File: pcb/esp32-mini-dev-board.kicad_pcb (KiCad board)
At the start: 2 copper layers, 39.9 x 52 mm, 11 parts, among them J1 USB_C_Receptacle_USB2.0_16P, U1 USBLC6-2SC6, U2 AP2112K-3.3, U3 ESP32-C3-WROOM-02

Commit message: feat(lay): add first placement of all parts
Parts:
- added C10: 100n, Capacitor_SMD:C_0603_1608Metric, B.Cu at (157.0, 100.9)
- added C11: C, Capacitor_SMD:C_0603_1608Metric, F.Cu at (173.2, 125.4)
- added C5: C, Capacitor_SMD:C_0603_1608Metric, B.Cu at (161.6, 99.7)
- added C6: 4u7, Capacitor_SMD:C_0603_1608Metric, F.Cu at (162.1, 117.8)
- added C7: C, Capacitor_SMD:C_0603_1608Metric, B.Cu at (161.5, 102.3)
- added C8: 4u7, Capacitor_SMD:C_0603_1608Metric, F.Cu at (159.6, 114.6)
- added C9: 4u7, Capacitor_SMD:C_0603_1608Metric, B.Cu at (157.1, 99.2)
- added J2: Conn_01x08_Pin, Connector_PinHeader_2.54mm:PinHeader_1x08_P2.54mm_Vertical, B.Cu at (150.0, 100.0)
- added J3: Conn_01x08_Pin, Connector_PinHeader_2.54mm:PinHeader_1x08_P2.54mm_Vertical, B.Cu at (176.0, 100.0)
- added R10: R, Resistor_SMD:R_0603_1608Metric, F.Cu at (154.0, 114.9)
- added R11: R, Resistor_SMD:R_0603_1608Metric, F.Cu at (173.2, 127.2)
- added R3: R, Resistor_SMD:R_0603_1608Metric, F.Cu at (150.6, 123.6)
- added R4: R, Resistor_SMD:R_0603_1608Metric, F.Cu at (149.7, 121.2)
- added R5: 0R, Resistor_SMD:R_0603_1608Metric, F.Cu at (160.9, 119.5)
- added R6: 0R, Resistor_SMD:R_0603_1608Metric, B.Cu at (168.8, 100.3)
- added R7: R, Resistor_SMD:R_0603_1608Metric, B.Cu at (166.5, 101.1)
- added R8: 0R, Resistor_SMD:R_0603_1608Metric, B.Cu at (168.8, 101.8)
- added R9: R, Resistor_SMD:R_0603_1608Metric, F.Cu at (171.8, 114.8)
- added SW1: SW_Push, Button_Switch_SMD:SW_SPST_B3U-1000P, F.Cu at (153.0, 130.0)
- added SW2: SW_Push, Button_Switch_SMD:SW_SPST_B3U-1000P, F.Cu at (173.0, 130.0)
- added Y1: Crystal, Crystal:Crystal_SMD_3215-2Pin_3.2x1.5mm, B.Cu at (164.3, 101.0)
- C1: value 4u7 -> C; footprint Diode_SMD:D_SMA -> Capacitor_SMD:C_0603_1608Metric
- C2: footprint Diode_SMD:D_SMA -> Capacitor_SMD:C_0603_1608Metric
- C3: value 4u7 -> C; footprint Package_TO_SOT_SMD:SOT-23-5 -> Capacitor_SMD:C_0603_1608Metric
- C4: footprint Package_TO_SOT_SMD:SOT-23-5 -> Capacitor_SMD:C_0603_1608Metric
- R1, R2: footprint Resistor_SMD:R_0402_1005Metric -> Resistor_SMD:R_0603_1608Metric
- moved J1 37.2 mm to (163.0, 131.0)
- moved U2 35.5 mm to (162.2, 114.7), turned to 90 degrees
- moved U3 32.2 mm to (163.0, 104.7)
- moved U1 26.2 mm to (162.7, 122.9), turned to 90 degrees
- moved C2 25.6 mm to (157.6, 121.2), turned to 180 degrees
- moved D1 25.0 mm to (154.1, 122.1), turned to 90 degrees
- moved C4 21.6 mm to (157.6, 119.5), turned to 180 degrees
- moved R1 19.3 mm to (165.3, 124.4), turned to 90 degrees
- moved R2 15.1 mm to (160.1, 124.4), turned to 90 degrees
- moved C1 14.5 mm to (149.7, 126.0), turned to 180 degrees
- moved C3 9.33 mm to (149.0, 123.6), turned to -90 degrees
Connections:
- net Net-(U2-EN) renamed +5V
- C1 pad 1: Net-(D1-A1) -> Net-(C1-Pad1)
- C2 pad 1: Net-(C2-Pad1) -> Net-(D1-A1)
- C3 pad 1: Net-(U2-VOUT) -> /CIRCUIT DESIGN/EN_RST
- U1 pad 4: USB_D+ -> /CIRCUIT DESIGN/USB_D+
- U1 pad 6: USB_D- -> /CIRCUIT DESIGN/USB_D-
- U2 pad 5: Net-(U2-VOUT) -> +3V3
- U3 pad 1: unconnected-(U3-3V3-Pad1) -> +3V3
- U3 pad 10: unconnected-(U3-IO10-Pad10) -> /CIRCUIT DESIGN/IO10
- U3 pad 11: unconnected-(U3-IO20/RXD-Pad11) -> /CIRCUIT DESIGN/RXD
- U3 pad 12: unconnected-(U3-IO21/TXD-Pad12) -> /CIRCUIT DESIGN/TXD
- U3 pad 13: unconnected-(U3-IO18-Pad13) -> /CIRCUIT DESIGN/USB_D-
- U3 pad 14: unconnected-(U3-IO19-Pad14) -> /CIRCUIT DESIGN/USB_D+
- U3 pad 15: unconnected-(U3-IO3-Pad15) -> /CIRCUIT DESIGN/IO3
- U3 pad 16: unconnected-(U3-IO2-Pad16) -> Net-(U3-IO2)
- U3 pad 17: unconnected-(U3-IO1-Pad17) -> /CIRCUIT DESIGN/XTAL_32K_N
- U3 pad 18: unconnected-(U3-IO0-Pad18) -> /CIRCUIT DESIGN/XTAL_32K_P
- U3 pad 19: Net-(U3-GND-Pad19) -> GND
- U3 pad 2: unconnected-(U3-EN-Pad2) -> /CIRCUIT DESIGN/EN
- U3 pad 3: unconnected-(U3-IO4-Pad3) -> /CIRCUIT DESIGN/IO4
- U3 pad 4: unconnected-(U3-IO5-Pad4) -> /CIRCUIT DESIGN/IO5
- U3 pad 5: unconnected-(U3-IO6-Pad5) -> /CIRCUIT DESIGN/IO6
- U3 pad 6: unconnected-(U3-IO7-Pad6) -> /CIRCUIT DESIGN/IO7
- U3 pad 7: unconnected-(U3-IO8-Pad7) -> Net-(U3-IO8)
- U3 pad 8: unconnected-(U3-IO9-Pad8) -> /CIRCUIT DESIGN/BOOT
- U3 pad 9: Net-(U3-GND-Pad19) -> GND
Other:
- board size 39.9 x 52 mm -> 31 x 37.4 mm

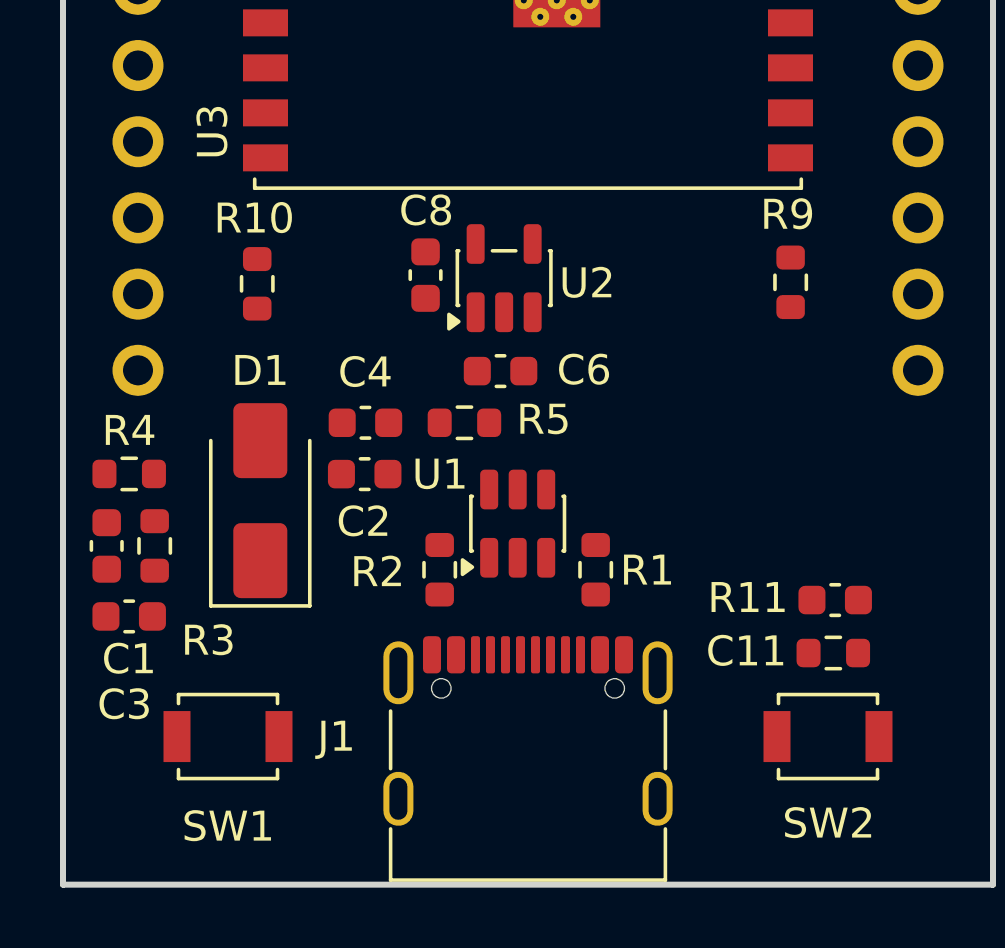
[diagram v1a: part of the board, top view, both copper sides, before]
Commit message: feat(lay): modify placement and first pre-routing
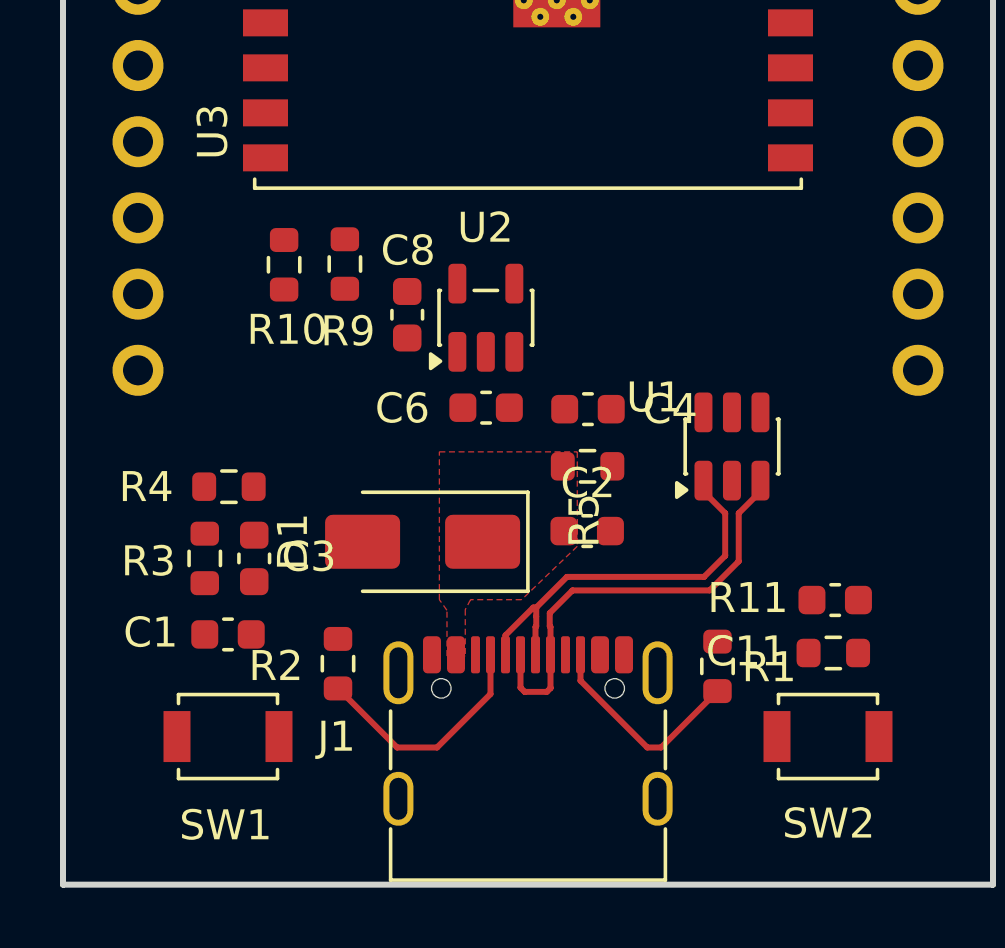
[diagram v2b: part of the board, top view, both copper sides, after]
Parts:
- moved R9 14.9 mm to (156.9, 114.2), turned to 90 degrees
- moved C2 7.66 mm to (165.0, 123.1), turned to 0 degrees
- moved U1 7.59 mm to (169.8, 120.3)
- moved C4 7.43 mm to (165.0, 119.1), turned to 0 degrees
- moved D1 5.58 mm to (159.5, 123.5), turned to 180 degrees
- moved R1 5.18 mm to (169.3, 127.6)
- moved C3 4.94 mm to (153.9, 124.0)
- moved R2 4.61 mm to (156.7, 127.6)
- moved R5 4.35 mm to (165.0, 121.0), turned to 0 degrees
- moved R4 3.35 mm to (153.0, 121.7), turned to 180 degrees
- moved C1 3.35 mm to (153.0, 126.6), turned to 0 degrees
- moved R3 1.72 mm to (152.2, 124.0)
- moved C8 1.45 mm to (159.0, 115.9)
- moved U2 1.45 mm to (161.6, 116.0)
- moved C6 1.31 mm to (161.6, 119.0), turned to 180 degrees
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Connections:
- net Net-(D1-A1) renamed /CIRCUIT DESIGN/VBUS
- R11 pad 1: +VDD -> +3V3
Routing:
- net /CIRCUIT DESIGN/D+: track 0.00 -> 14.7 mm
- net /CIRCUIT DESIGN/D-: track 0.00 -> 13.5 mm
- net Net-(J1-CC1): track 0.00 -> 7.95 mm
- net Net-(J1-CC2): track 0.00 -> 7.13 mm
- added copper zone on F.Cu, net /CIRCUIT DESIGN/VBUS

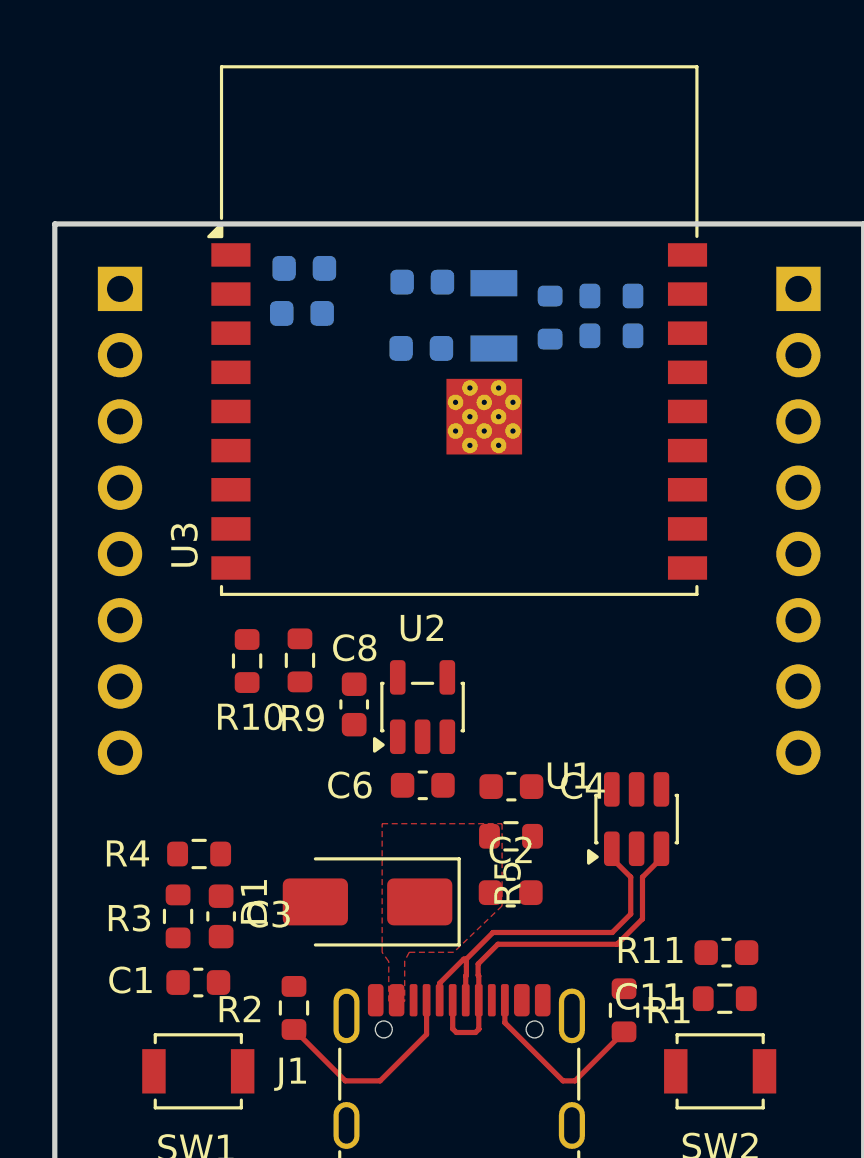
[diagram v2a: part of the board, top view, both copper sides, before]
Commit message: feat(lay/pwr): add +3V3 power zones in F.Cu
- Design rules were set to meet the JLCPCB manufacturing capabilities.
- The +5 and VBUS power zones in F.Cu were fixed to pass DRC.
- Vias for GND, +5V, +3V3 and VBUS were added.
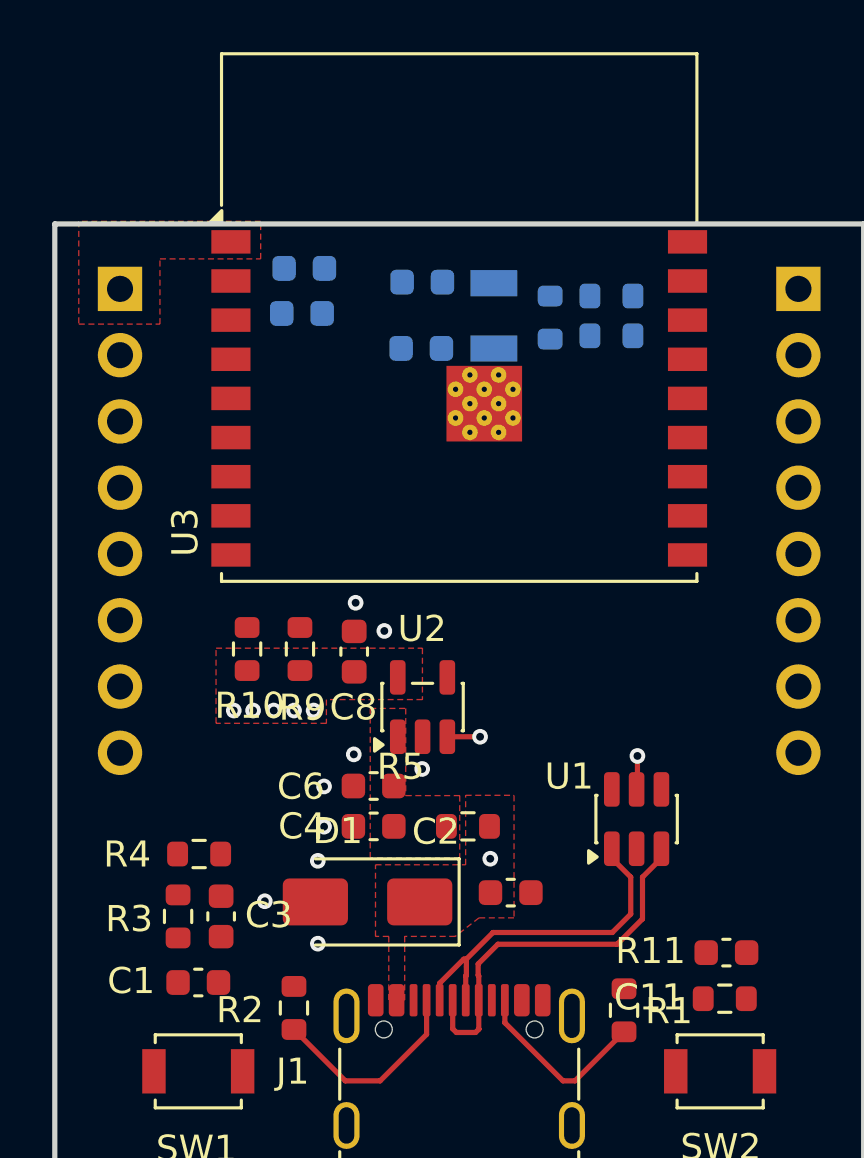
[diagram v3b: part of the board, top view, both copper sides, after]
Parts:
- moved C4 5.49 mm to (159.7, 120.6), turned to 180 degrees
- moved C8 2.03 mm to (159.0, 113.9), turned to 90 degrees
- moved C6 1.88 mm to (159.7, 119.1)
- moved R5 1.69 mm to (163.3, 120.6), turned to 180 degrees
- moved U3 0.50 mm to (163.0, 104.2)
- moved R10 0.46 mm to (154.9, 113.8)
- moved R9 0.43 mm to (156.9, 113.8)
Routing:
- net /CIRCUIT DESIGN/VBUS: track 0.00 -> 1.30 mm, vias 0 -> 2
- net +5V: track 0.00 -> 1.26 mm, vias 0 -> 1
- net GND: vias 0 -> 9
- net +3V3: vias 0 -> 5
- added copper zone on F.Cu, net +3V3
- added copper zone on F.Cu, net +5V
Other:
- copper layers 2 -> 4

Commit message: feat(lay/mcu): add copper zones to connect +3V3 pads to bypass capacitors
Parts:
- moved C10 2.99 mm to (155.0, 98.7)
- moved C9 2.38 mm to (155.0, 100.5)
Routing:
- net +3V3: vias 5 -> 9
- added copper zone on B.Cu, net +3V3
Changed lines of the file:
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@@
 		(capping no)
 		(filling no)
-		(zone_defaults)
 		(pcbplotparams
 			(layerselection 0x00000000_00000000_55555555_5755f5ff)
@@
 	(footprint "Capacitor_SMD:C_0603_1608Metric"
 		(layer "B.Cu")
-		(at 157.0612 99.2126)
+		(at 155.04 100.46)
 		(descr "Capacitor SMD 0603 (1608 Metric), square (rectangular) end terminal, IPC-7351 nominal, (Body size source: IPC-SM-782 page 76, https://www.pcb-3d.com/wordpress/wp-content/uploads/ipc-sm-782a_amendment_1_and_2.pdf)")
 		(tags "capacitor")
@@
 	(footprint "Capacitor_SMD:C_0603_1608Metric"
 		(layer "B.Cu")
-		(at 156.9726 100.9398)
+		(at 155.04 98.6598)
 		(descr "Capacitor SMD 0603 (1608 Metric), square (rectangular) end terminal, IPC-7351 nominal, (Body size source: IPC-SM-782 page 76, https://www.pcb-3d.com/wordpress/wp-content/uploads/ipc-sm-782a_amendment_1_and_2.pdf)")
 		(tags "capacitor")
@@
 	)
 	(via
+		(at 152.84 98.07)
+		(size 0.6)
+		(drill 0.3)
+		(layers "F.Cu" "B.Cu")
+		(free yes)
+		(net "+3V3")
+	)
+	(via
 		(at 157.42 116.16)
 		(size 0.6)
@@
 	)
 	(via
+		(at 152.09 98.07)
+		(size 0.6)
+		(drill 0.3)
+		(layers "F.Cu" "B.Cu")
+		(free yes)
+		(net "+3V3")
+	)
+	(via
 		(at 155.1 116.16)
 		(size 0.6)
@@
 	)
 	(via
+		(at 152.86 98.79)
+		(size 0.6)
+		(drill 0.3)
+		(layers "F.Cu" "B.Cu")
+		(free yes)
+		(net "+3V3")
+	)
+	(via
 		(at 155.89 116.16)
 		(size 0.6)
@@
 	)
 	(via
+		(at 152.09 98.74)
+		(size 0.6)
+		(drill 0.3)
+		(layers "F.Cu" "B.Cu")
+		(free yes)
+		(net "+3V3")
+	)
+	(via
 		(at 154.36 116.16)
 		(size 0.6)
@@
 		(polygon
 			(pts
-				(xy 157.91 115.74) (xy 157.91 116.65) (xy 153.68 116.65) (xy 153.68 113.77) (xy 161.59 113.77) (xy 161.59 115.74)
+				(xy 157.91 115.74) (xy 157.91 116.87) (xy 153.68 116.87) (xy 153.68 113.77) (xy 161.59 113.77) (xy 161.59 115.74)
 			)
 		)
@@
 		(polygon
 			(pts
-				(xy 148.42 97.41) (xy 148.42 101.35) (xy 151.53 101.35) (xy 151.53 98.85) (xy 155.39 98.85) (xy 155.39 97.41)
+				(xy 148.42 97.41) (xy 148.42 101.35) (xy 151.91 101.35) (xy 151.91 99.15) (xy 156.31 99.15) (xy 156.31 97.41)
 			)
 		)
@@
 			)
 		)
+	)
+	(zone
+		(net "+3V3")
+		(layer "B.Cu")
+		(hatch none 0.5)
+		(priority 5)
+		(connect_pads
+			(clearance 0)
+		)
+		(min_thickness 0.2)
+		(fill yes
+			(thermal_gap 0.15)
+			(thermal_bridge_width 0.25)
+			(smoothing fillet)
+			(radius 0.5)
+			(island_removal_mode 1)
+		)
+		(polygon
+			(pts
+				(xy 157.95 116.825) (xy 157.95 115.55) (xy 155.15 115.55) (xy 155.15 101.325) (xy 151.375 101.325)
+				(xy 151.75 101.325) (xy 151.75 116.825)
+			)
+		)
+	)
+	(zone
+		(net "+3V3")
+		(layer "B.Cu")
+		(hatch none 0.5)
+		(priority 4)
+		(connect_pads
+			(clearance 0)
+		)
+		(min_thickness 0.2)
+		(fill yes
+			(thermal_gap 0.15)
+			(thermal_bridge_width 0.25)
+			(smoothing fillet)
+			(radius 0.5)
+			(island_removal_mode 1)
+		)
+		(polygon
+			(pts
+				(xy 155.15 101.325) (xy 155.15 97.7) (xy 148.025 97.7) (xy 148.025 101.325)
+			)
+		)

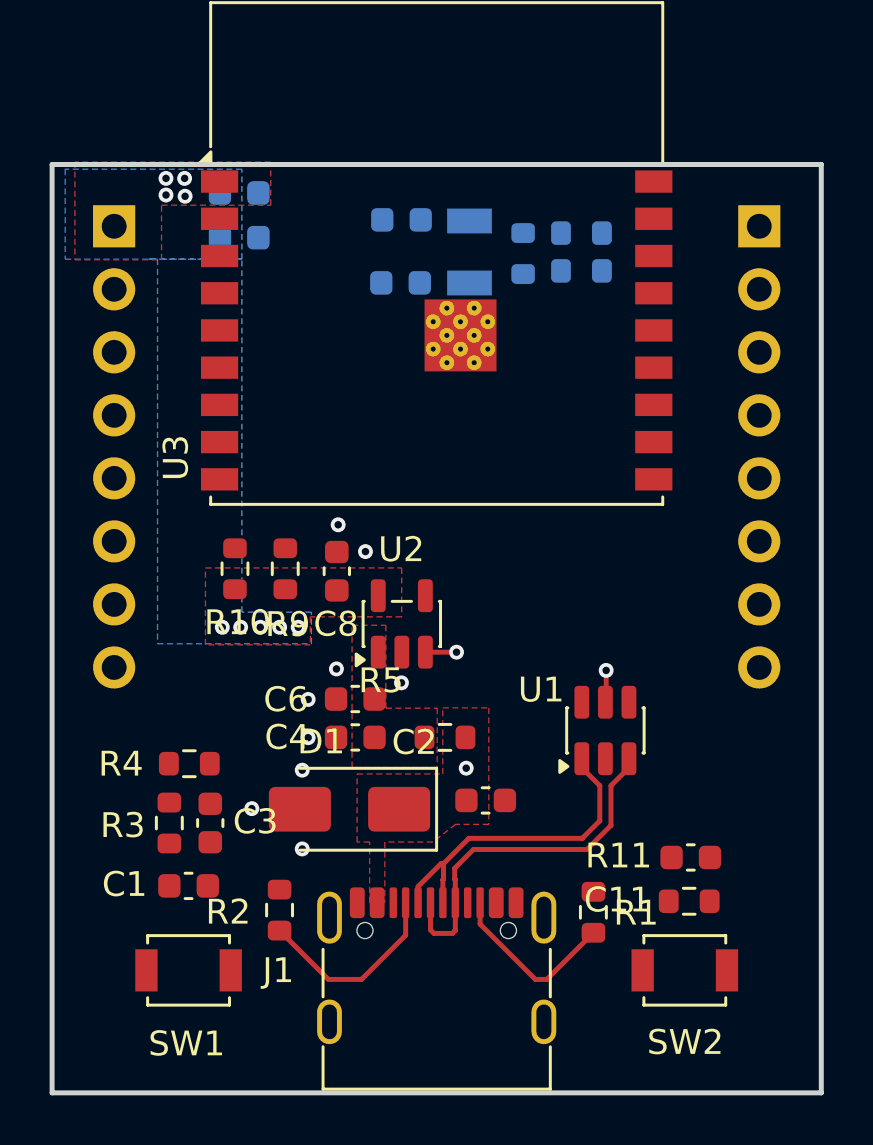
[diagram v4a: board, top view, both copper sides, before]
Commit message: feat(lay/usb): add differential pair tracks
The JLCPCB stackup was modified to allow thinner differential tracks.
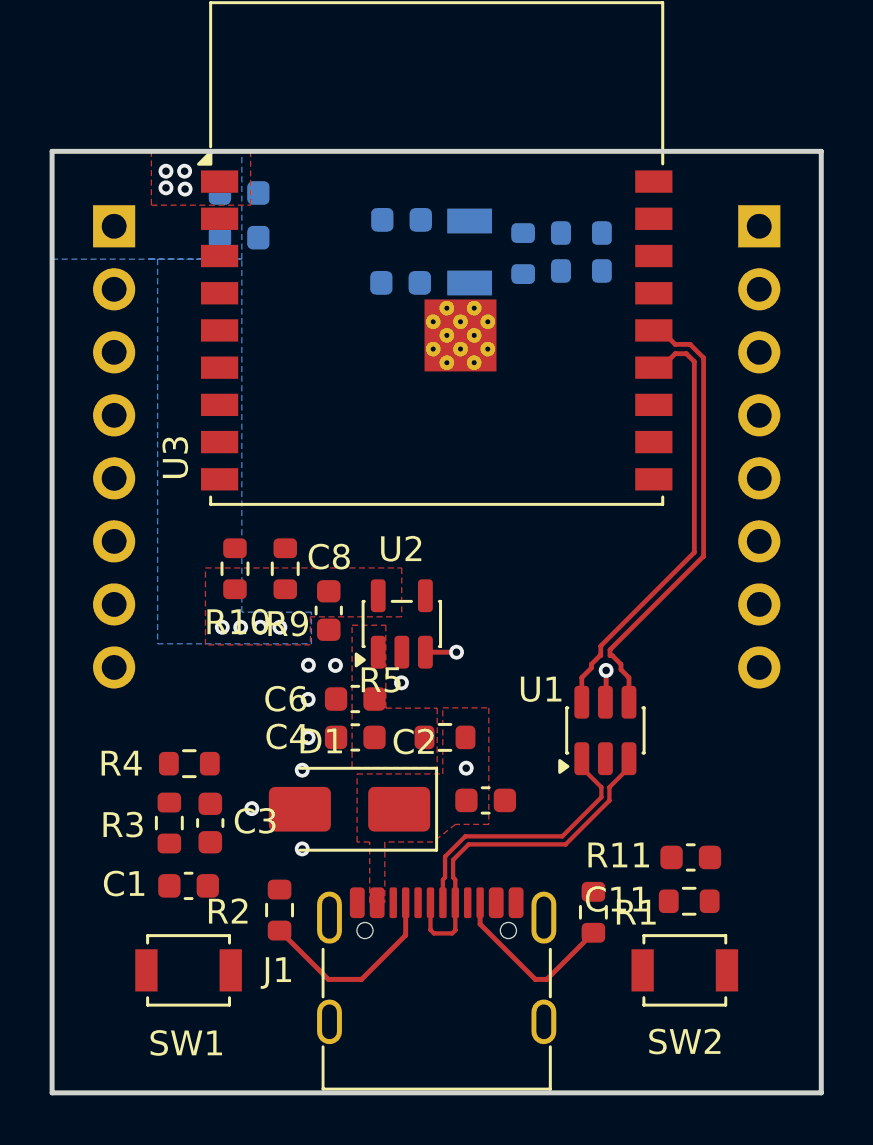
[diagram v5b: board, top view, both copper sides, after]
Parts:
- moved C8 1.62 mm to (158.7, 115.5), turned to -90 degrees
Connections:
- net /CIRCUIT DESIGN/D+ renamed /CIRCUIT DESIGN/USB_IN+
- net /CIRCUIT DESIGN/D- renamed /CIRCUIT DESIGN/USB_IN-
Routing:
- net /CIRCUIT DESIGN/USB_D+: track 0.00 -> 18.3 mm
- net /CIRCUIT DESIGN/USB_D-: track 0.00 -> 17.6 mm
- net /CIRCUIT DESIGN/USB_IN-: track 13.5 -> 11.1 mm
- net GND: vias 9 -> 8
- net +3V3: vias 9 -> 8
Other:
- board size 31 x 37.4 mm -> 31 x 37.9 mm
